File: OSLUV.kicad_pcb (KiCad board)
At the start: 4 copper layers, 110 x 85 mm, 222 parts, among them IC1 NCP12510ASN65T1G, IC2 SFH6156-3, IC3 INA210, IC4 AP63300WU-7, IC5 AP63300WU-7, IC6 STM32G071KBT6, IC7 TLV9001IDBVR, IC8 1ED44175N01BXTSA1, IC9 LP2985-33DBVR, J1 B08B-XASK-1-A_LF__SN_, J3 BM02B-SRSS-TB_LF__SN_, J4 BM02B-SRSS-TB_LF__SN_, J5 640445-2, J6 640445-2, J7 B5P-VH, Q1 STD3NK80ZT4, Q2 BC847, Q3 BSS138, Q4 BC807, Q6 BC847, T1 T_NMOS_DSKG, U1 OPA2356AIDGKR, U2 AZ431LANTR, U3 LM2901, U4 Prog

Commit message: Rev. 1.0.0 production data
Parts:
- removed the C17 at (116.0, 119.8)
- removed the C46 at (123.1, 105.6)
- removed the C47 at (127.3, 102.0)
- removed the C5 at (61.0, 121.2)
- removed the D15 at (122.2, 123.5)
- removed H5: MountingHole_Pad, Hansmann:Mounting_M3_NPTH_Vias
- removed the IC7 at (129.6, 105.8)
- removed the J4 at (125.5, 96.8)
- removed the R42 at (125.8, 102.0)
- removed the R43 at (124.2, 102.0)
- removed the R56 at (101.2, 107.5)
- removed the R67 at (106.5, 113.8)
- removed the R68 at (110.3, 117.5)
- removed the R69 at (108.8, 117.5)
- removed U4: Prog, Hansmann:Prog_St
- added C28: 100n 0603, Capacitor_SMD:C_0603_1608Metric, F.Cu at (139.2, 103.9)
- added C29: 100n 0603, Capacitor_SMD:C_0603_1608Metric, F.Cu at (137.7, 103.9)
- added C42: 220µ 35V, Capacitor_THT:CP_Radial_D8.0mm_P3.50mm, F.Cu at (101.0, 132.5)
- added C44: 100n 0603, Capacitor_SMD:C_0805_2012Metric, F.Cu at (111.0, 132.5)
- added C56: 10µ X7R 50V 1210, Capacitor_SMD:C_1210_3225Metric, F.Cu at (101.0, 130.7)
- added D16: BAT54J, Hansmann_Dioden:D_SOD-323F, F.Cu at (122.2, 119.2)
- added D18: BAT54J, Hansmann_Dioden:D_SOD-323F, F.Cu at (123.2, 106.2)
- added F2: Polyfuse 200 mA, Fuse:Fuse_1206_3216Metric, F.Cu at (134.4, 100.7)
- added J3: TC2030, Connector:Tag-Connect_TC2030-IDC-NL_2x03_P1.27mm_Vertical_beidseitig, F.Cu at (133.6, 115.9)
- added J5: B4B-PH-K-S_LF__SN_, Hansmann_Kontakte:B4B-PH-K-S, F.Cu at (129.0, 96.5)
- added L2: L, Inductor_SMD:L_0805_2012Metric, F.Cu at (134.9, 102.7)
- added Q5: DCX114EU-7-F, Hansmann_AD-DA:SOT65P210X110-6N, F.Cu at (108.0, 113.2)
- added R28: 100R 0603, Hansmann_Resistor:R_0603_1608Metric, F.Cu at (125.8, 104.0)
- added R30: 100R 0603, Hansmann_Resistor:R_0603_1608Metric, F.Cu at (125.8, 102.5)
- added R31: 1k5 0603, Hansmann_Resistor:R_0603_1608Metric, F.Cu at (134.0, 111.8)
- added R34: 10k 0603, Hansmann_Resistor:R_0603_1608Metric, F.Cu at (118.5, 105.2)
- added R40: 2k2 0603, Hansmann_Resistor:R_0603_1608Metric, F.Cu at (129.4, 104.8)
- added R44: 100R 0603, Hansmann_Resistor:R_0603_1608Metric, F.Cu at (129.9, 101.0)
- added R45: 100R 0603, Hansmann_Resistor:R_0603_1608Metric, F.Cu at (131.4, 101.0)
- added R57: 100k 0603, Hansmann_Resistor:R_0603_1608Metric, F.Cu at (126.5, 106.2)
- added R59: 10k 0603, Hansmann_Resistor:R_0603_1608Metric, F.Cu at (119.8, 119.5)
- added R62: 1k 0603, Hansmann_Resistor:R_0603_1608Metric, F.Cu at (108.0, 115.3)
- added TP11: OCP, TestPoint:TestPoint_Pad_D1.0mm, F.Cu at (121.0, 106.5)
- added VR1: TC33X-2-103E, Hansmann_Potis:TC33X2503E, F.Cu at (121.8, 124.0)
- C10, C11, C12, C19, C20, C21: footprint Capacitor_SMD:C_1210_3225Metric -> Hansmann_Kondensatoren:C_1210_3225Metric
- C16: renamed from C27; footprint Capacitor_SMD:C_1210_3225Metric -> Hansmann_Kondensatoren:C_1210_3225Metric
- C17: renamed from C28; footprint Capacitor_SMD:C_1210_3225Metric -> Hansmann_Kondensatoren:C_1210_3225Metric
- C2: renamed from C110; value 330µ 35V -> 100µ 35V; footprint Capacitor_THT:CP_Radial_D8.0mm_P5.00mm -> Capacitor_THT:CP_Radial_D8.0mm_P3.50mm
- C30: renamed from C34; footprint Capacitor_SMD:C_1210_3225Metric -> Hansmann_Kondensatoren:C_1210_3225Metric
- C31: renamed from C35; footprint Capacitor_SMD:C_1210_3225Metric -> Hansmann_Kondensatoren:C_1210_3225Metric
- C36: renamed from C38; footprint Capacitor_SMD:C_1210_3225Metric -> Hansmann_Kondensatoren:C_1210_3225Metric
- C37: renamed from C39; footprint Capacitor_SMD:C_1210_3225Metric -> Hansmann_Kondensatoren:C_1210_3225Metric
- C39: renamed from C1; footprint Capacitor_SMD:C_1210_3225Metric -> Hansmann_Kondensatoren:C_1210_3225Metric
- C43: renamed from C50; footprint Capacitor_SMD:C_1210_3225Metric -> Hansmann_Kondensatoren:C_1210_3225Metric
- C45: renamed from C52; footprint Capacitor_SMD:C_1210_3225Metric -> Hansmann_Kondensatoren:C_1210_3225Metric
- C47: renamed from C53; footprint Capacitor_SMD:C_1210_3225Metric -> Hansmann_Kondensatoren:C_1210_3225Metric
- C5: renamed from C26; footprint Capacitor_SMD:C_1210_3225Metric -> Hansmann_Kondensatoren:C_1210_3225Metric
- C51: renamed from C58; value 1n8 1% C0G 0603 -> 1n 1% C0G 0603
- C55: renamed from C4; value 100n 0603 -> 1u 0603
- C57: value 10p 1% 600V 1206 -> 100p 0603; footprint Capacitor_SMD:C_1206_3216Metric -> Capacitor_SMD:C_0603_1608Metric
- D1, D3, D7: footprint Diode_SMD:D_SOD-323F -> Hansmann_Dioden:D_SOD-323F
- D11: value BAS40-04 -> LED rd 0603; footprint Package_TO_SOT_SMD:SOT-23 -> Hansmann_LED:LED_0603_1608Metric
- D12: renamed from D18; footprint LED_SMD:LED_0603_1608Metric -> Hansmann_LED:LED_0603_1608Metric
- D13, D14: value BAS40-04 -> D5V0P4UR6SO-7; footprint Package_TO_SOT_SMD:SOT-23 -> Hansmann_Dioden:SOT95P285X140-6N
- D15: renamed from D12; footprint LED_SMD:LED_0603_1608Metric -> Hansmann_LED:LED_0603_1608Metric
- D17: renamed from D10; footprint Diode_SMD:D_SOD-323F -> Hansmann_Dioden:D_SOD-323F
- D19: renamed from D16; footprint Diode_SMD:D_SOD-323F -> Hansmann_Dioden:D_SOD-323F
- D20: renamed from D17; footprint Diode_SMD:D_SOD-323F -> Hansmann_Dioden:D_SOD-323F
- D21: renamed from D22; footprint Diode_SMD:D_SOD-323F -> Hansmann_Dioden:D_SOD-323F
- J1: renamed from J6; value 640445-2 -> B04B-XASK-1_LF__SN_; footprint Hansmann:6404452 -> Hansmann_Kontakte:B04BXASK1LFSN
- J2: renamed from J1; footprint Hansmann:B08BXASK1ALFSN -> Connector_JST:JST_XA_B08B-XASK-1-A_1x08_P2.50mm_Vertical
- Q2: value BC847 -> DCX114EU-7-F; footprint Package_TO_SOT_SMD:SOT-23 -> Hansmann_AD-DA:SOT65P210X110-6N
- Q4: value BC807 -> DCX114EU-7-F; footprint Package_TO_SOT_SMD:SOT-23 -> Hansmann_AD-DA:SOT65P210X110-6N
- R12, R14, R15, R16, R17, R19, R20, R21, R22, R23, R24, R25, R6: footprint Resistor_SMD:R_0603_1608Metric -> Hansmann_Resistor:R_0603_1608Metric
- R27: renamed from R37; value 10k 0603 -> 1k 0603; footprint Resistor_SMD:R_0603_1608Metric -> Hansmann_Resistor:R_0603_1608Metric
- R29: value 10k 0603 -> 100R 0603; footprint Resistor_SMD:R_0603_1608Metric -> Hansmann_Resistor:R_0603_1608Metric
- R32: renamed from R64; footprint Resistor_SMD:R_0603_1608Metric -> Hansmann_Resistor:R_0603_1608Metric
- R33: renamed from R36; footprint Resistor_SMD:R_0603_1608Metric -> Hansmann_Resistor:R_0603_1608Metric
- R36: renamed from R72; footprint Resistor_SMD:R_0603_1608Metric -> Hansmann_Resistor:R_0603_1608Metric
- R37: renamed from R39; footprint Resistor_SMD:R_0603_1608Metric -> Hansmann_Resistor:R_0603_1608Metric
- R38: renamed from R40; footprint Resistor_SMD:R_0603_1608Metric -> Hansmann_Resistor:R_0603_1608Metric
- R39: renamed from R35; footprint Resistor_SMD:R_0603_1608Metric -> Hansmann_Resistor:R_0603_1608Metric
- R41: value 10k 0603 -> 2k2 0603; footprint Resistor_SMD:R_0603_1608Metric -> Hansmann_Resistor:R_0603_1608Metric
- R42: renamed from R34; value 180R 0805 -> 680R 0805
- R43: renamed from R33; value 180R 0805 -> 680R 0805
- R46: renamed from R31; footprint Resistor_SMD:R_0603_1608Metric -> Hansmann_Resistor:R_0603_1608Metric
- R47: renamed from R28; footprint Resistor_SMD:R_0603_1608Metric -> Hansmann_Resistor:R_0603_1608Metric
- R48: renamed from R78; footprint Resistor_SMD:R_0603_1608Metric -> Hansmann_Resistor:R_0603_1608Metric
- R49: renamed from R32; footprint Resistor_SMD:R_0603_1608Metric -> Hansmann_Resistor:R_0603_1608Metric
- R50: renamed from R30; footprint Resistor_SMD:R_0603_1608Metric -> Hansmann_Resistor:R_0603_1608Metric
- R51: renamed from R38; footprint Resistor_SMD:R_0603_1608Metric -> Hansmann_Resistor:R_0603_1608Metric
- R52: renamed from R75; footprint Resistor_SMD:R_0603_1608Metric -> Hansmann_Resistor:R_0603_1608Metric
- R53: renamed from R76; footprint Resistor_SMD:R_0603_1608Metric -> Hansmann_Resistor:R_0603_1608Metric
- R54: renamed from R44; footprint Resistor_SMD:R_0603_1608Metric -> Hansmann_Resistor:R_0603_1608Metric
- R55: renamed from R60; footprint Resistor_SMD:R_0603_1608Metric -> Hansmann_Resistor:R_0603_1608Metric
- R56: renamed from R62; footprint Resistor_SMD:R_0603_1608Metric -> Hansmann_Resistor:R_0603_1608Metric
- R58: renamed from R63; footprint Resistor_SMD:R_0603_1608Metric -> Hansmann_Resistor:R_0603_1608Metric
- R61: renamed from R50; footprint Resistor_SMD:R_0603_1608Metric -> Hansmann_Resistor:R_0603_1608Metric
- R64: renamed from R51; footprint Resistor_SMD:R_0603_1608Metric -> Hansmann_Resistor:R_0603_1608Metric
- R69: renamed from R57; value 5k6 0.1% 0603 -> 12k 0.1% 0603; footprint Resistor_SMD:R_0603_1608Metric -> Hansmann_Resistor:R_0603_1608Metric
- R72: renamed from R53; footprint Resistor_SMD:R_0603_1608Metric -> Hansmann_Resistor:R_0603_1608Metric
- R73: renamed from R70; footprint Resistor_SMD:R_0603_1608Metric -> Hansmann_Resistor:R_0603_1608Metric
- R74: renamed from R71; footprint Resistor_SMD:R_0603_1608Metric -> Hansmann_Resistor:R_0603_1608Metric
- R75: renamed from R73; footprint Resistor_SMD:R_0603_1608Metric -> Hansmann_Resistor:R_0603_1608Metric
- R76: renamed from R58; footprint Resistor_SMD:R_0603_1608Metric -> Hansmann_Resistor:R_0603_1608Metric
- R77: renamed from R65; footprint Resistor_SMD:R_0603_1608Metric -> Hansmann_Resistor:R_0603_1608Metric
- R78: renamed from R59; footprint Resistor_SMD:R_0603_1608Metric -> Hansmann_Resistor:R_0603_1608Metric
- R79: renamed from R61; footprint Resistor_SMD:R_0603_1608Metric -> Hansmann_Resistor:R_0603_1608Metric
- R80: renamed from R66; value 3k9 0603 -> 18k 0603; footprint Resistor_SMD:R_0603_1608Metric -> Hansmann_Resistor:R_0603_1608Metric
- R81: renamed from R77; value 100k 0603 -> DNP; footprint Resistor_SMD:R_0603_1608Metric -> Hansmann_Resistor:R_0603_1608Metric
- R82: renamed from R74; value 1k 0603 -> 10k 0603; footprint Resistor_SMD:R_0603_1608Metric -> Hansmann_Resistor:R_0603_1608Metric
- moved R43 39.9 mm to (98.2, 101.2)
- moved R42 39.7 mm to (98.5, 103.2), turned to 180 degrees
- moved TP5 38.3 mm to (102.2, 99.0)
- moved Q3 37.5 mm to (101.8, 102.2)
- moved R39 32.5 mm to (104.3, 103.8), turned to 90 degrees
- moved J4 32.5 mm to (100.0, 96.7)
- moved D11 17.7 mm to (135.5, 111.8), turned to 90 degrees
- moved R27 17.5 mm to (135.9, 105.0), turned to -90 degrees
- moved Q2 15.5 mm to (118.3, 103.0), turned to 180 degrees
- moved R29 14.6 mm to (115.8, 105.5)
- moved C57 13.8 mm to (113.2, 117.2)
- moved TH1 13.7 mm to (117.2, 122.2), turned to 0 degrees
- moved C40 13.2 mm to (116.0, 132.2)
- moved TP8 11.5 mm to (116.0, 123.8)
- moved R33 11.3 mm to (133.2, 119.0), turned to 180 degrees
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- renumbered C43 to C1, C29 to C24, C31 to C25, C45 to C26, C2 to C27, C42 to C3, C36 to C34, C37 to C35, C6 to C38, C44 to C4, C49 to C40, C3 to C41, C61 to C46, C51 to C48, C55 to C49, C56 to C50, C40 to C52, C59 to C53, C30 to C6, D21 to D10, F2 to F1, F1 to F3, IC6 to IC3, IC3 to IC4, IC4 to IC5, IC5 to IC6, IC9 to IC7, J3 to J4, J7 to J6, L3 to L1, L4 to L3, L5 to L4, L6 to L5, L1 to L6, R27 to R35, R47 to R60, R46 to R63, R49 to R65, R48 to R66, R54 to R67, R55 to R68, R79 to R70, R52 to R71, J5 to ST2, TP14 to TP10, TP2 to TP12, TP11 to TP13, TP12 to TP14, TP4 to TP2, TP5 to TP4, TP6 to TP5, TP9 to TP6, TP8 to TP7, TP10 to TP8, TP13 to TP9, U3 to U1, U1 to U3
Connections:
- net /excimerDriver/lampDriver/Lamp_HV renamed /excimerDriver/lampDriver/HV_Lamp
- net Net-(IC6-PC15-OSC32_OUT) renamed /excimerDriver/LED1
- C51 pad 1: /excimerDriver/lampDriver/HV_Drain_div3 -> /excimerDriver/lampDriver/HV_Drain_div2
- C57 pad 1: /excimerDriver/lampDriver/HV_Drain_div2 -> /excimerDriver/Isense_MOS
- C57 pad 2: /excimerDriver/lampDriver/HV_Drain_div3 -> GND
- D11 pad 2: +3V3 -> Net-(D11-A)
- D13 pad 1: GND -> /excimerDriver/Status
- D13 pad 2: Net-(IC6-PA9) -> GND
- D13 pad 3: Net-(C46-Pad1) -> /excimerDriver/PWM
- D14 pad 1: GND -> unconnected-(D14-I/O1-Pad1)
- D14 pad 2: +3V3 -> GND
- D14 pad 3: /excimerDriver/LampIntensity/UV_Sensor -> /excimerDriver/MCU_REMOTE
- IC3 pad 10: /excimerDriver/Usense_Lamp -> /excimerDriver/CMD_RX
- IC3 pad 11: unconnected-(IC6-PA4-Pad11) -> /excimerDriver/UV_LED
- IC3 pad 16: /excimerDriver/LampIntensity -> /excimerDriver/Usense_Lamp
- IC3 pad 19: Net-(IC6-PA9) -> unconnected-(IC3-PA9-Pad19)
- IC3 pad 2: unconnected-(IC6-PC14-OSC32_IN-Pad2) -> /excimerDriver/LED2
- IC3 pad 20: /excimerDriver/AlivePWM -> /excimerDriver/OCP_RESET
- IC3 pad 22: unconnected-(IC6-PA11_[PA9]-Pad22) -> /excimerDriver/I2C_SCL
- IC3 pad 23: unconnected-(IC6-PA12_[PA10]-Pad23) -> /excimerDriver/I2C_SDA
- IC3 pad 26: /excimerDriver/CMD_RX -> unconnected-(IC3-PD0-Pad26)
- IC3 pad 30: /excimerDriver/UV_LED -> unconnected-(IC3-PB6-Pad30)
- IC3 pad 32: /excimerDriver/DRV_Mask -> unconnected-(IC3-PB8-Pad32)
- IC8 pad 5: /excimerDriver/OCP -> Net-(D18-A)
- J1 pad 2: GND -> /excimerDriver/!REMOTE
- J2 pad 4: /excimerDriver/Enable -> /excimerDriver/!REMOTE
- J2 pad 5: /excimerDriver/Status -> /excimerDriver/Lamp_on_status
- J2 pad 6: /excimerDriver/PWM -> Net-(J2-Pad6)
- J2 pad 7: /excimerDriver/CMD_TX -> Net-(J2-Pad7)
- J2 pad 8: /excimerDriver/CMD_RX -> Net-(J2-Pad8)
- Q2 pad 1: Net-(Q2-B) -> GND
- Q2 pad 2: GND -> /excimerDriver/Status
- Q2 pad 3: /excimerDriver/OCP -> unconnected-(Q2-OUT2-Pad3)
- Q4 pad 1: Net-(Q4-B) -> GND
- Q4 pad 2: +3V3 -> /excimerDriver/OCP_RESET
- Q4 pad 3: Net-(Q4-C) -> unconnected-(Q4-OUT2-Pad3)
- R27 pad 2: /excimerDriver/Enable -> /excimerDriver/!REMOTE
- R29 pad 1: Net-(Q4-C) -> Net-(J2-Pad6)
- R29 pad 2: Net-(Q2-B) -> /excimerDriver/PWM
- R41 pad 1: Net-(IC6-PA9) -> /excimerDriver/I2C_SCL
- R41 pad 2: GND -> +3V3
- R69 pad 1: /excimerDriver/lampDriver/HV_Drain_div3 -> /excimerDriver/lampDriver/HV_Drain_div2
- U1 pad 13: /excimerDriver/OCP -> Net-(D18-A)
- U3 pad 5: /excimerDriver/lampDriver/HV_Drain_div3 -> /excimerDriver/lampDriver/HV_Drain_div2
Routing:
- net /excimerDriver/24V_FUSE: track 30.1 -> 84.2 mm, vias 1 -> 2
- net /excimerDriver/Lamp_on_status: track 0.00 -> 46.0 mm, vias 0 -> 2
- net /excimerDriver/!REMOTE: track 0.00 -> 45.3 mm, vias 0 -> 1
- net Net-(D18-A): track 0.00 -> 42.1 mm, vias 0 -> 2
- net /excimerDriver/lampDriver/HV_Drain: track 5.70 -> 35.7 mm, vias 54 -> 1
- net /excimerDriver/temp_MOSFET: track 60.8 -> 33.1 mm, vias 6 -> 4
- net GND: track 203.4 -> 177.0 mm, vias 102 -> 97
- net /excimerDriver/VDC_filter: track 51.6 -> 26.2 mm, vias 0 -> 2
- net /excimerDriver/I2C_SDA: track 0.00 -> 24.4 mm, vias 0 -> 2
- net /excimerDriver/VDC: track 137.2 -> 114.7 mm
- net /excimerDriver/OCP: track 46.4 -> 25.0 mm, vias 6 -> 3
- net /excimerDriver/I2C_SCL: track 0.00 -> 21.2 mm, vias 0 -> 2
- net /excimerDriver/OCP_RESET: track 0.00 -> 20.7 mm, vias 0 -> 2
- net /excimerDriver/CMD_RX: track 25.5 -> 7.18 mm, vias 2 -> 0
- net /excimerDriver/SWDIO: track 4.95 -> 23.1 mm, vias 1 -> 2
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- added copper zone on In2.Cu, net /excimerDriver/lampDriver/VDC_Trafo
- added copper zone on In2.Cu, net GND
- removed copper zone on In2.Cu, net +15V
- removed copper zone on F.Cu, net +3V3
- removed copper zone on B.Cu, net /excimerDriver/lampDriver/HV_Drain
- removed copper zone on F.Cu, net /excimerDriver/lampDriver/HV_Drain
- removed copper zone on In1.Cu, net /excimerDriver/lampDriver/HV_Drain
- removed copper zone on In2.Cu, net /excimerDriver/lampDriver/HV_Drain
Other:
- outline, holes or cut-outs redrawn
- board text added: "!REMOTE"
- board text added: "+3V3"
- board text added: "18V"
- board text added: "24V"
- board text added: "24V_power"
- board text added: "24V_sense"
- board text added: "All dimensions in mm."
- board text added: "All mounting points M3."
- board text added: "DGND"
- board text added: "Fail"
- board text added: "HV OUT"
- board text added: "Lamp_on"
- board text added: "OSLUV Excimer Driver Rev 1.0.0 25/11/19"
- board text added: "PGND"
- board text added: "PWM"
- board text added: "Temp"
- board text added: "Trim"
- board text added: "UART_RX"
- board text added: "UART_TX"
- board text added: "UV LED"
- board text added: "i2c CLK"
- board text added: "i2c DAT"
- board text added: "iIn"
- board text added: "iLa"
- board text added: "iMOS"
- board text added: "uG"
- board text added: "uLa"
- board text removed: "DNP"
- board text removed: "LED"
- board text removed: "OSLUV Excimer Driver V2 25/08/10"
- board text removed: "Sensor"
- board text removed: "Status"

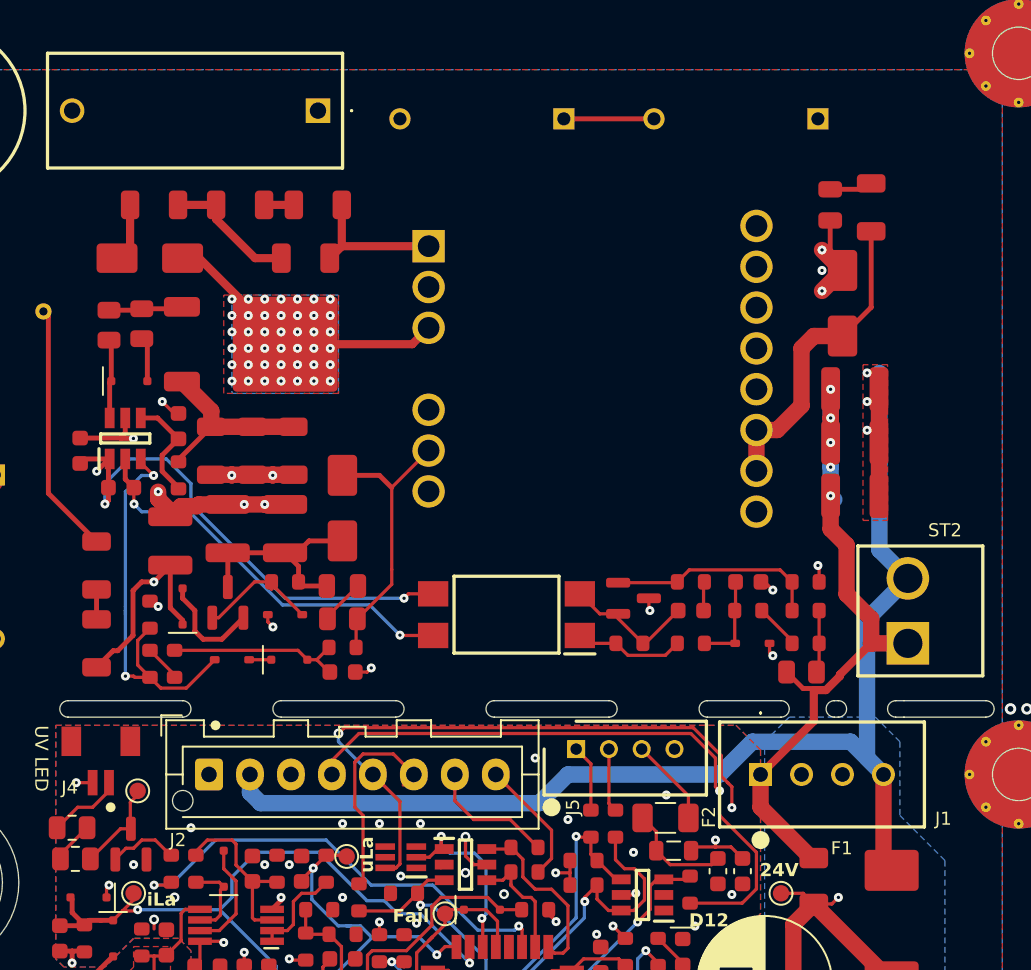
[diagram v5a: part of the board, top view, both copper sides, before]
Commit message: Rev 1.0.0 corrected component values
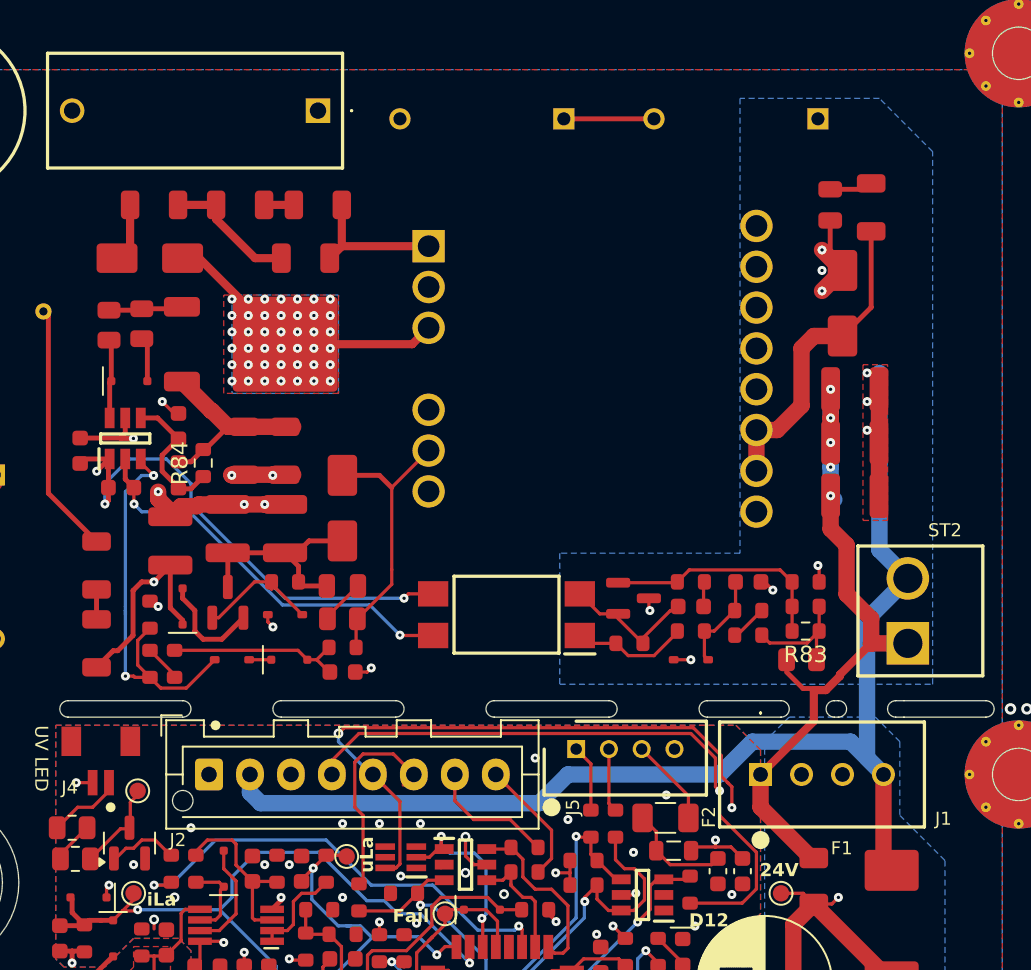
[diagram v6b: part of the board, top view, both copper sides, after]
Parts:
- removed R3: 1R8 5% 1206, Resistor_SMD:R_1206_3216Metric
- added R83: 100k 0603, Resistor_SMD:R_0603_1608Metric, F.Cu at (143.0, 89.2)
- added R84: 56k 0603, Resistor_SMD:R_0603_1608Metric, F.Cu at (106.2, 79.0)
- C10: value 10u 50V X7R 1210 -> 2u2 50V X7R 1210
- C13: value 220p 250V X7R 0805 -> 220p 100V X7R 0805
- C15, C8: value 100nF 0603 -> 100n 0603
- C7: value 100pF NP0 0603 -> 33pF NP0 0603
- C9: value 100pF NP0 1206 -> 10n 1210
- D8: value RGF1M -> BX320_R1
- Q3: value BSS138 -> BC817-40
- R1: value 1R8 5% 1206 -> 0R47 5% 1206
- R10, R9: value 20k 1206 -> 330k 1206
- R15: value 30k1 0603 -> 2k2 0603
- R16: value 220k 0603 -> 390k 0603
- R2: value 1R8 5% 1206 -> 1R 5% 1206
- R24: value 86k6 0603 -> 680k 0603
- R39: value 10R 0603 -> 1k 0603
- R56: value 2k2 0603 -> 3k3 0603
- R59: value 10k 0603 -> 5k6 0603
- R6: value 300R 0603 -> 6k8 0603
- R7, R8: value 820k 1206 -> 390k 1206
- R80: value 18k 0603 -> 22k 0603
- moved D9 3.88 mm to (136.0, 91.0), turned to 180 degrees
- moved R22 3.54 mm to (139.5, 89.5)
- moved R1 2.01 mm to (108.8, 78.2)
- moved R2 2.01 mm to (111.2, 78.2)
- moved R19 0.75 mm to (136.0, 89.2)
- moved R26 0.75 mm to (142.8, 91.0)
- moved C23 0.25 mm to (136.0, 87.8)
- moved R24 0.25 mm to (143.0, 87.8)
- moved Q3 0.11 mm to (101.8, 102.2)
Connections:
- L104 pad 12: unconnected-(L104-N2_2.1-Pad12) -> GND
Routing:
- net Net-(R22-Pad1): track 4.05 -> 7.55 mm
- net Net-(IC1-CS): track 6.71 -> 8.53 mm
- net Net-(U2-REF): track 13.0 -> 14.5 mm
- net GNDS: track 64.6 -> 63.4 mm
- net Net-(Q1-S): track 11.5 -> 12.0 mm
